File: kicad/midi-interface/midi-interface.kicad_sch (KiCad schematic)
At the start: 3 parts, among them J1 Conn_01x05_Pin, U1 ATmega328P-P, Y1 Crystal

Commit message: midi interface kicad update
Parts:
- removed J1: Conn_01x05_Pin, symbol Connector:Conn_01x05_Pin
- removed U1: ATmega328P-P, Package_DIP:DIP-28_W7.62mm, symbol MCU_Microchip_ATmega:ATmega328P-P
- removed Y1: Crystal, symbol Device:Crystal
- added C1: 0.1u, Capacitor_SMD:C_1206_3216Metric_Pad1.33x1.80mm_HandSolder, symbol Device:C
- added D1: 1N914, Diode_SMD:D_1206_3216Metric_Pad1.42x1.75mm_HandSolder, symbol Diode:1N914
- added J1: DIN-5, Connector_PinHeader_2.54mm:PinHeader_1x05_P2.54mm_Vertical, symbol Connector:DIN-5_180degree
- added J10: OUT9, Connector_Audio:Jack_3.5mm_QingPu_WQP-PJ398SM_Vertical_CircularHoles, symbol Connector_Audio:AudioJack2
- added J11: OUT10, Connector_Audio:Jack_3.5mm_QingPu_WQP-PJ398SM_Vertical_CircularHoles, symbol Connector_Audio:AudioJack2
- added J12: OUT11, Connector_Audio:Jack_3.5mm_QingPu_WQP-PJ398SM_Vertical_CircularHoles, symbol Connector_Audio:AudioJack2
- added J13: OUT12, Connector_Audio:Jack_3.5mm_QingPu_WQP-PJ398SM_Vertical_CircularHoles, symbol Connector_Audio:AudioJack2
- added J14: Conn_02x08_Odd_Even, Connector_IDC:IDC-Header_2x08_P2.54mm_Vertical, symbol Connector_Generic:Conn_02x08_Odd_Even
- added J2: OUT1, Connector_Audio:Jack_3.5mm_QingPu_WQP-PJ398SM_Vertical_CircularHoles, symbol Connector_Audio:AudioJack2
- added J3: OUT2, Connector_Audio:Jack_3.5mm_QingPu_WQP-PJ398SM_Vertical_CircularHoles, symbol Connector_Audio:AudioJack2
- added J4: OUT3, Connector_Audio:Jack_3.5mm_QingPu_WQP-PJ398SM_Vertical_CircularHoles, symbol Connector_Audio:AudioJack2
- added J5: OUT4, Connector_Audio:Jack_3.5mm_QingPu_WQP-PJ398SM_Vertical_CircularHoles, symbol Connector_Audio:AudioJack2
- added J6: OUT5, Connector_Audio:Jack_3.5mm_QingPu_WQP-PJ398SM_Vertical_CircularHoles, symbol Connector_Audio:AudioJack2
- added J7: OUT6, Connector_Audio:Jack_3.5mm_QingPu_WQP-PJ398SM_Vertical_CircularHoles, symbol Connector_Audio:AudioJack2
- added J8: OUT7, Connector_Audio:Jack_3.5mm_QingPu_WQP-PJ398SM_Vertical_CircularHoles, symbol Connector_Audio:AudioJack2
- added J9: OUT8, Connector_Audio:Jack_3.5mm_QingPu_WQP-PJ398SM_Vertical_CircularHoles, symbol Connector_Audio:AudioJack2
- added JP1: Jumper_Programming, Connector_PinHeader_2.54mm:PinHeader_1x02_P2.54mm_Vertical, symbol Jumper:Jumper_2_Bridged
- added R1: 270R, Resistor_SMD:R_1206_3216Metric_Pad1.30x1.75mm_HandSolder, symbol Device:R
- added R2: 220R, Resistor_SMD:R_1206_3216Metric_Pad1.30x1.75mm_HandSolder, symbol Device:R
- added U1: EL817, Package_DIP:DIP-4_W7.62mm, symbol Isolator:EL817
- added XA2: Arduino_Nano_Socket, arduino:Arduino_Nano_Socket, symbol arduino:Arduino_Nano_Socket
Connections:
- net +5V: now also J14.11 (Pin_11), J14.12 (Pin_12), R1.1, XA2.5V
- net GND: now also C1.1, J10.S, J11.S, J12.S, J13.S, J14.3 (Pin_3), J14.4 (Pin_4), J14.5 (Pin_5), J14.6 (Pin_6), J14.7 (Pin_7), J14.8 (Pin_8), J2.S, J3.S, J4.S, J5.S, J6.S, J7.S, J8.S, J9.S, U1.3, XA2.GND1 (GND), XA2.GND2 (GND)
- new net: J11.T, XA2.D11 (D11_MOSI)
- new net: J2.T, XA2.D2 (D2_INT0)
- new net: J10.T, XA2.D10
- new net: JP1.1 (A), R1.2, U1.4
- new net: J13.T, XA2.D13 (D13_SCK)
- new net: JP1.2 (B), XA2.D0 (D0/RX)
- new net: J12.T, XA2.D12 (D12_MISO)
- new net: J3.T, XA2.D3 (D3_INT1)
- new net: J4.T, XA2.D4
- new net: J5.T, XA2.D5
- new net: J6.T, XA2.D6
- new net: J7.T, XA2.D7
- new net: J8.T, XA2.D8
- new net: J9.T, XA2.D9
- new net: C1.2, J1.2
- new net: J1.4, R2.1
- new net: D1.1 (K), R2.2, U1.1
- new net: D1.2 (A), J1.5, U1.2
- new net +12V: J14.10 (Pin_10), J14.9 (Pin_9)
- new net -12V: J14.1 (Pin_1), J14.2 (Pin_2)
- no-connect marks 0 -> 20

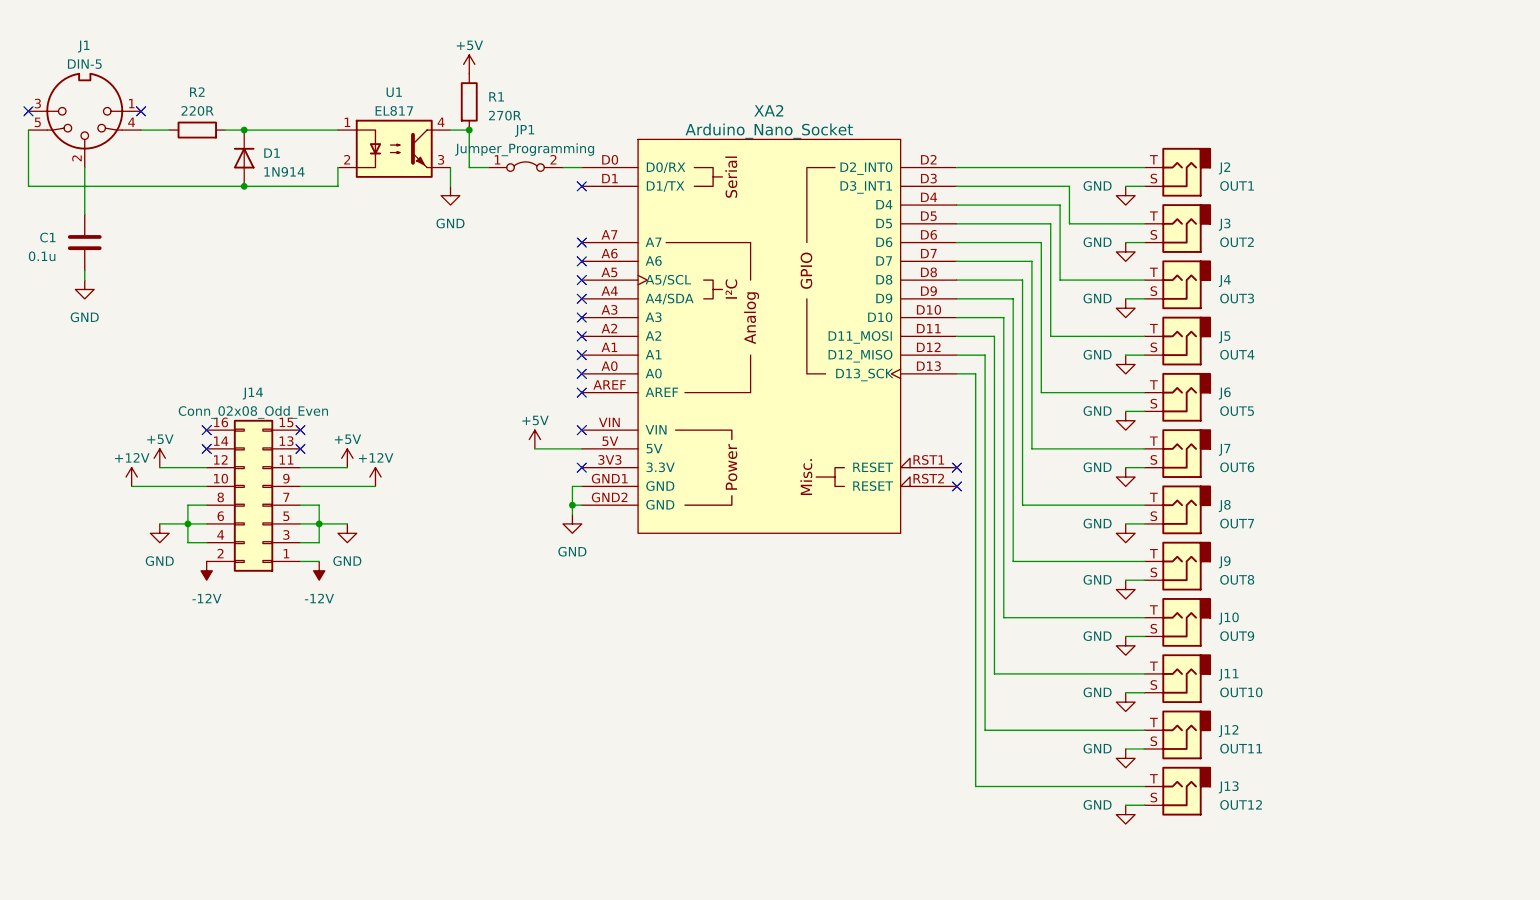
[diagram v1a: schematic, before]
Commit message: update midi interface layout
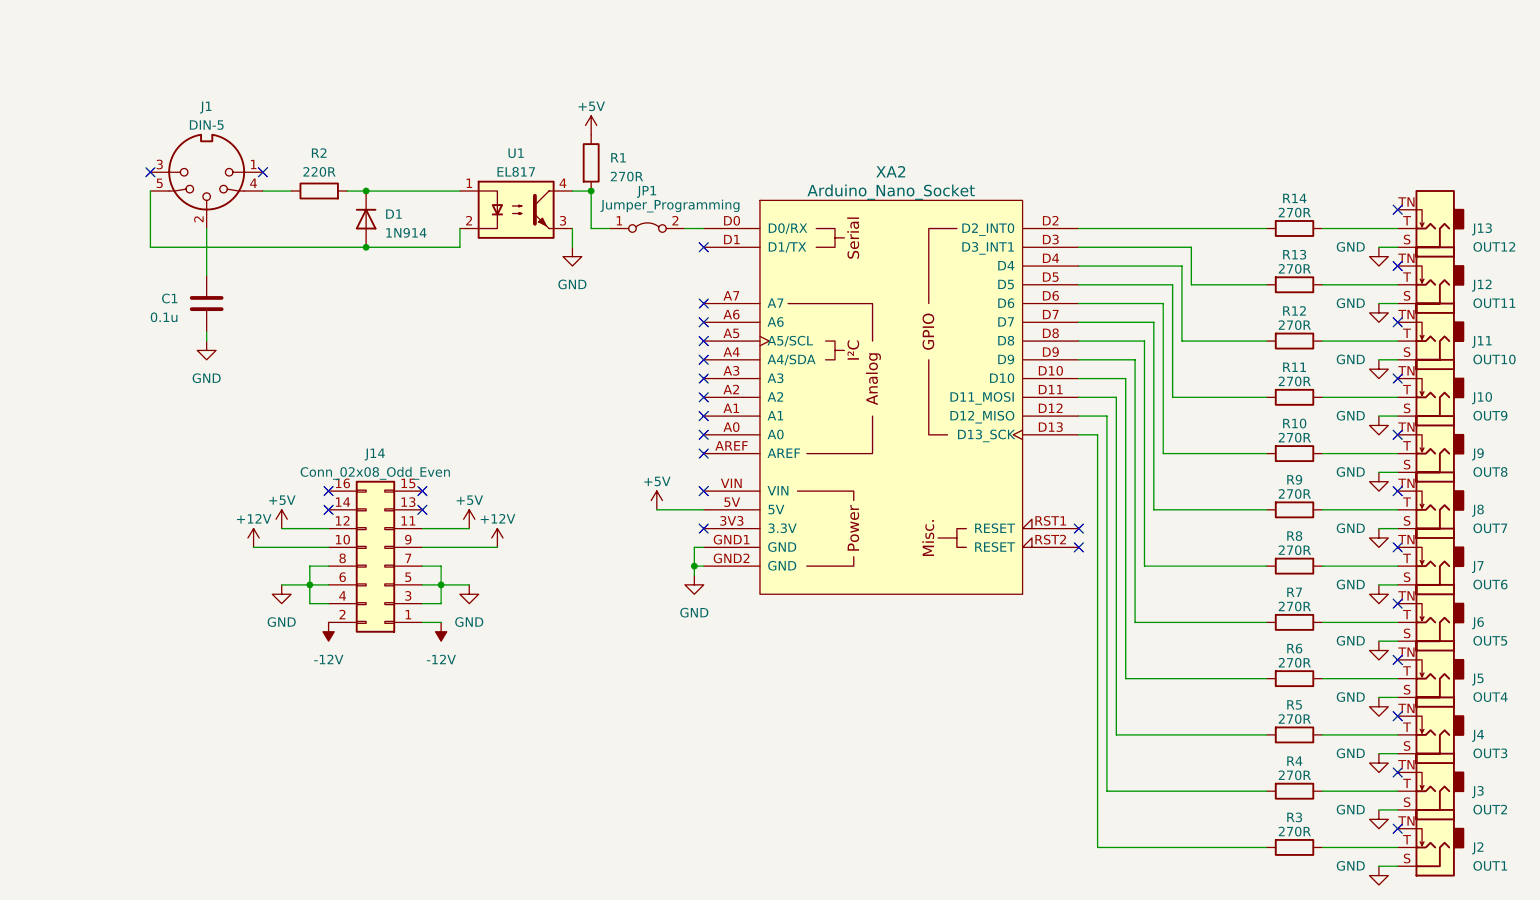
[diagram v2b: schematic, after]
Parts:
- added R10, R11, R12, R13, R14, R3, R4, R5, R6, R7, R8, R9: 270R, Resistor_SMD:R_1206_3216Metric_Pad1.30x1.75mm_HandSolder, symbol Device:R
- J10, J11, J12, J13, J2, J3, J4, J5, J6, J7, J8, J9: symbol Connector_Audio:AudioJack2 -> Connector_Audio:AudioJack2_SwitchT
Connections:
- net at J11.T: now also R12.1; no longer XA2.D11 (D11_MOSI)
- net at J2.T: now also R3.1; no longer XA2.D2 (D2_INT0)
- net at J10.T: now also R11.1; no longer XA2.D10
- net at J13.T: now also R14.1; no longer XA2.D13 (D13_SCK)
- net at XA2.D12 (D12_MISO): now also R4.2; no longer J12.T
- net at XA2.D3 (D3_INT1): now also R13.2; no longer J3.T
- net at XA2.D4: now also R12.2; no longer J4.T
- net at XA2.D5: now also R11.2; no longer J5.T
- net at XA2.D6: now also R10.2; no longer J6.T
- net at J7.T: now also R8.1; no longer XA2.D7
- net at XA2.D8: now also R8.2; no longer J8.T
- net at XA2.D9: now also R7.2; no longer J9.T
- new net: R14.2, XA2.D2 (D2_INT0)
- new net: R6.2, XA2.D10
- new net: R5.2, XA2.D11 (D11_MOSI)
- new net: R3.2, XA2.D13 (D13_SCK)
- new net: R9.2, XA2.D7
- new net: J8.T, R9.1
- new net: J3.T, R4.1
- new net: J5.T, R6.1
- new net: J6.T, R7.1
- new net: J9.T, R10.1
- new net: J4.T, R5.1
- new net: J12.T, R13.1
- no-connect marks 20 -> 32
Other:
- moved on the sheet: C1, D1, J1, J14, JP1, R1, R2, U1, XA2

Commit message: fertiggestellte midi Platine, Frontplatte für midi interface
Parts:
- removed U1: EL817, Package_DIP:DIP-4_W7.62mm, symbol Isolator:EL817
- removed XA2: Arduino_Nano_Socket, arduino:Arduino_Nano_Socket, symbol arduino:Arduino_Nano_Socket
- added U2: 6N136, Package_DIP:DIP-8_W7.62mm, symbol Isolator:6N136
- added XA1: Arduino_Uno_R3_SMD_Shield, arduino:Arduino_Uno_R3_Shield, symbol arduino:Arduino_Uno_R3_SMD_Shield
- D1: footprint Diode_SMD:D_1206_3216Metric_Pad1.42x1.75mm_HandSolder -> Diode_THT:D_DO-41_SOD81_P5.08mm_Vertical_AnodeUp
- R1: value 270R -> 560R
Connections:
- net +5V: now also U2.8, XA1.5V1 (5V)
- net GND: now also U2.5, XA1.GND1 (GND), XA1.GND2 (GND), XA1.GND3 (GND)
- net at R11.2: now also XA1.D13
- net at R14.2: now also XA1.D10 (D10_CS)
- net at JP1.1 (A), R1.2: now also U2.6
- net at R12.2: now also XA1.D12
- net at R8.2: now also XA1.D8
- net at JP1.2 (B): now also XA1.D0 (D0/RX)
- net at R6.2: now also XA1.D2 (D2_INT0)
- net at R5.2: now also XA1.D3 (D3_INT1)
- net at R4.2: now also XA1.D4
- net at R3.2: now also XA1.D5
- net at R13.2: now also XA1.D11
- net at R10.2: now also XA1.D6
- net at R9.2: now also XA1.D7
- net at R7.2: now also XA1.D9
- net at D1.1 (K), R2.2: now also U2.2
- net at D1.2 (A), J1.5: now also U2.3
- no-connect marks 32 -> 39
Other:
- moved on the sheet: J10, J11, J12, J13, J2, J3, J4, J5, R1, R11, R12, R13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
